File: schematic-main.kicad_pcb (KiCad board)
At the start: 2 copper layers, 100 x 100 mm, 145 parts, among them IC1 LM76202QPWPRQ1, IC2 AD8544ARUZ-REEL, IC3 ACHS-7123-000E, IC4 ACHS-7121-000E, IC5 ACHS-7123-000E, IC6 LM5106MMX_NOPB, J1 Battery converter, J2 CAN, J3 FUEL CELL, J4 Joulemeter, J5 MOTOR CONTROLER, J6 SUPER CAPACITORS, P1 USB_C_Plug_USB2.0, Q1 CSD19531Q5AT, Q2 CSD19531Q5AT, U1 TPS62933, U2 USBLC6-2P6, U3 ESP32-S3FN8, U4 SN65HVD232, Y1 Crystal_GND24

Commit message: Buck - boost converter
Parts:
- added C16: 100n, Capacitor_SMD:C_1206_3216Metric, F.Cu at (40.3, 160.3)
- added C17: 1u, Capacitor_SMD:C_1206_3216Metric, F.Cu at (35.0, 160.3)
- added C18: 1u, Capacitor_SMD:C_1206_3216Metric, F.Cu at (105.1, 133.8)
- added C22: 100n, Capacitor_SMD:C_1206_3216Metric, F.Cu at (28.2, 159.0)
- added C23: 100n, Capacitor_SMD:C_1206_3216Metric, F.Cu at (28.0, 164.0)
- added C24: 100n, Capacitor_SMD:C_1206_3216Metric, F.Cu at (31.9, 165.3)
- added C25: 1u, Capacitor_SMD:C_1206_3216Metric, F.Cu at (39.1, 174.5)
- added C26: 10n, Capacitor_SMD:C_1206_3216Metric, F.Cu at (44.0, 160.1)
- added C27: 4n7, Capacitor_SMD:C_1206_3216Metric, F.Cu at (30.7, 159.0)
- added C28: 100n, Capacitor_SMD:C_1206_3216Metric, F.Cu at (25.7, 159.0)
- added C31: 100n, Capacitor_SMD:C_1206_3216Metric, F.Cu at (123.4, 104.3)
- added C34: 1n, Capacitor_SMD:C_1206_3216Metric, F.Cu at (104.9, 99.6)
- added C47: 470n, Capacitor_SMD:C_1206_3216Metric, F.Cu at (238.5, 111.3)
- added C48: 10n, Capacitor_SMD:C_1206_3216Metric, F.Cu at (238.5, 114.6)
- added C49: 100n 100V, Capacitor_SMD:C_1206_3216Metric, F.Cu at (238.5, 118.0)
- added D10: 1N4148, Diode_THT:D_DO-35_SOD27_P7.62mm_Horizontal, F.Cu at (231.6, 100.7)
- added D11: 1N4148, Diode_THT:D_DO-35_SOD27_P7.62mm_Horizontal, F.Cu at (231.6, 104.3)
- added D12: 1N4148, Diode_THT:D_DO-35_SOD27_P7.62mm_Horizontal, F.Cu at (231.6, 107.8)
- added D4: LED, Package_TO_SOT_SMD:SOT-323_SC-70, F.Cu at (104.6, 95.4)
- added D5: LED, LED_SMD:LED_1206_3216Metric, F.Cu at (52.2, 165.3)
- added D6: LED, LED_SMD:LED_1206_3216Metric, F.Cu at (52.3, 168.4)
- added IC7: LM5106MMX_NOPB, Lib:SOP50P490X110-10N, F.Cu at (223.8, 117.3)
- added L3: 700uH, Inductor_SMD:L_0402_1005Metric, F.Cu at (30.8, 163.1)
- added Q3: CSD19531Q5AT, Lib:CSD19531Q5AT, F.Cu at (152.1, 92.9)
- added Q4: CSD19531Q5AT, Lib:CSD19531Q5AT, F.Cu at (163.9, 98.1)
- added R1: 5k1, Resistor_SMD:R_1206_3216Metric, F.Cu at (109.9, 138.8)
- added R2: 0, Resistor_SMD:R_1206_3216Metric, F.Cu at (105.2, 138.1)
- added R25: 10k, Resistor_SMD:R_1206_3216Metric, F.Cu at (26.1, 171.5)
- added R26: 10k, Resistor_SMD:R_1206_3216Metric, F.Cu at (26.1, 174.5)
- added R27: 20k, Resistor_SMD:R_1206_3216Metric, F.Cu at (30.0, 177.1)
- added R28: 10k, Resistor_SMD:R_1206_3216Metric, F.Cu at (33.1, 180.4)
- added R29: 20k, Resistor_SMD:R_1206_3216Metric, F.Cu at (35.2, 177.5)
- added R3: 0, Resistor_SMD:R_1206_3216Metric, F.Cu at (102.4, 138.1)
- added R30: 10k, Resistor_SMD:R_1206_3216Metric, F.Cu at (38.1, 180.5)
- added R31: 20k, Resistor_SMD:R_1206_3216Metric, F.Cu at (106.5, 102.2)
- added R32: 68k, Resistor_SMD:R_1206_3216Metric, F.Cu at (109.5, 104.7)
- added R35: 100R 0,5W, Resistor_SMD:R_1206_3216Metric, F.Cu at (57.5, 165.3)
- added R36: 100R 0,5W, Resistor_SMD:R_1206_3216Metric, F.Cu at (57.5, 168.4)
- added R4: 5k1, Resistor_SMD:R_1206_3216Metric, F.Cu at (97.6, 138.8)
- added R43: 100R, Resistor_SMD:R_1206_3216Metric, F.Cu at (242.9, 126.8)
- added R44: 10k, LED_SMD:LED_1206_3216Metric, F.Cu at (242.9, 123.5)
- added R45: 10R 2W, LED_SMD:LED_1206_3216Metric, F.Cu at (232.9, 111.3)
- added R46: 10k, LED_SMD:LED_1206_3216Metric, F.Cu at (232.9, 114.7)
- added R47: 10R 2W, Resistor_SMD:R_1206_3216Metric, F.Cu at (54.7, 160.2)
- added R48: 200R, Resistor_SMD:R_1206_3216Metric, F.Cu at (48.9, 160.1)
- added R49: 200R, LED_SMD:LED_1206_3216Metric, F.Cu at (232.9, 118.1)
- added R50: 0R, LED_SMD:LED_1206_3216Metric, F.Cu at (203.4, 67.2)
- added R51: 0R, LED_SMD:LED_1206_3216Metric, F.Cu at (203.4, 70.6)
- added TP10: I/O 2, Connector_PinSocket_2.54mm:PinSocket_1x01_P2.54mm_Vertical, F.Cu at (21.2, 169.8)
- added TP11: I/O 3, Connector_PinSocket_2.54mm:PinSocket_1x01_P2.54mm_Vertical, F.Cu at (21.2, 174.0)
- added TP12: I/O 4, Connector_PinSocket_2.54mm:PinSocket_1x01_P2.54mm_Vertical, F.Cu at (22.5, 178.0)
- added TP13: FC test, Connector_PinSocket_2.54mm:PinSocket_1x01_P2.54mm_Vertical, F.Cu at (26.5, 180.5)
- added TP20: I/O 4, Connector_PinSocket_2.54mm:PinSocket_1x01_P2.54mm_Vertical, F.Cu at (248.0, 127.5)
- added TP21: EN test, Connector_PinSocket_2.54mm:PinSocket_1x01_P2.54mm_Vertical, F.Cu at (243.1, 101.3)
- added TP22: PWM test, Connector_PinSocket_2.54mm:PinSocket_1x01_P2.54mm_Vertical, F.Cu at (243.1, 105.9)
- added U4: SN65HVD232, Package_DFN_QFN:QFN-56-1EP_7x7mm_P0.4mm_EP5.6x5.6mm, F.Cu at (39.8, 167.4)
- added U5: SN65HVD232, Package_SO:SOIC-8_3.9x4.9mm_P1.27mm, F.Cu at (116.7, 106.1)
- added Y1: Crystal_GND24, library:KC3225K400000C1GE00, F.Cu at (39.0, 156.6)
- J2: footprint Lib:39303035 -> library:39303035
- U3: footprint Package_DFN_QFN:QFN-56-1EP_7x7mm_P0.4mm_EP5.6x5.6mm -> Package_TO_SOT_SMD:SOT-666
- moved C32 29.0 mm to (150.5, 60.5)
- moved C45 21.5 mm to (151.0, 104.3), turned to 180 degrees
- moved L1 19.5 mm to (112.7, 75.3)
- moved U1 19.5 mm to (111.4, 80.3)
- moved U3 14.0 mm to (103.6, 130.8), turned to -90 degrees
- moved IC5 10.9 mm to (167.9, 125.2), turned to -90 degrees
- moved Q1 10.2 mm to (162.3, 73.1), turned to 90 degrees
- moved IC3 8.91 mm to (165.0, 109.4), turned to 90 degrees
- moved Q2 4.72 mm to (151.8, 73.1)
- moved F2 3.04 mm to (180.0, 122.0)
- moved J1 2.55 mm to (98.8, 80.0)
- moved J2 2.00 mm to (98.8, 97.4)
- moved P1 0.12 mm to (103.9, 145.9)
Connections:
- net /Converter/Bootstrap renamed /Converter/Bootstrap_A
- net /Converter/High_mosfet renamed /Converter/High_mosfet_A
- net /Converter/Low_mosfet renamed /Converter/Low_mosfet_A
- C44 pad 1: /Converter/SC_c2 -> /Converter/Bootstrap_B
- L3 pad 2: /Converter/SC_c2 -> /Converter/Bootstrap_B
- R35 pad 1: /Converter/SC_c2 -> /Converter/Bootstrap_B
- R39 pad 1: /Converter/Converter_ON_MCU -> /Converter/Converter_ON_B_MCU
- R40 pad 2: /Converter/Converter_PWM_MCU -> /Converter/Converter_PWM_B_MCU
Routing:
- net GND: track 0.00 -> 193.8 mm, vias 0 -> 25
- net (no net): track 0.00 -> 126.2 mm, vias 0 -> 9
- net +3.3V: track 0.00 -> 114.6 mm, vias 0 -> 5
- net /Converter/MC_c2: track 0.00 -> 90.6 mm
- net /Converter/SC_c2: track 0.00 -> 84.8 mm
- net /Converter/MC_c1: track 0.00 -> 50.8 mm
- net /Converter/FC_c1: track 0.00 -> 46.1 mm
- net /Converter/SC_c1: track 0.00 -> 45.7 mm
- net /IO/CAN_TX: track 0.00 -> 37.3 mm, vias 0 -> 1
- net /IO/CANH: track 0.00 -> 35.6 mm, vias 0 -> 1
- net unconnected-(U4-NC-Pad8): track 0.00 -> 34.3 mm, vias 0 -> 1
- net /IO/FC_Voltage_MCU: track 0.00 -> 32.1 mm, vias 0 -> 1
- net /Converter/FC_c2: track 0.00 -> 28.0 mm
- net /VBUS: track 0.00 -> 26.7 mm, vias 0 -> 2
- net /IO/CAN_RX: track 0.00 -> 21.1 mm
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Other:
- outline, holes or cut-outs redrawn

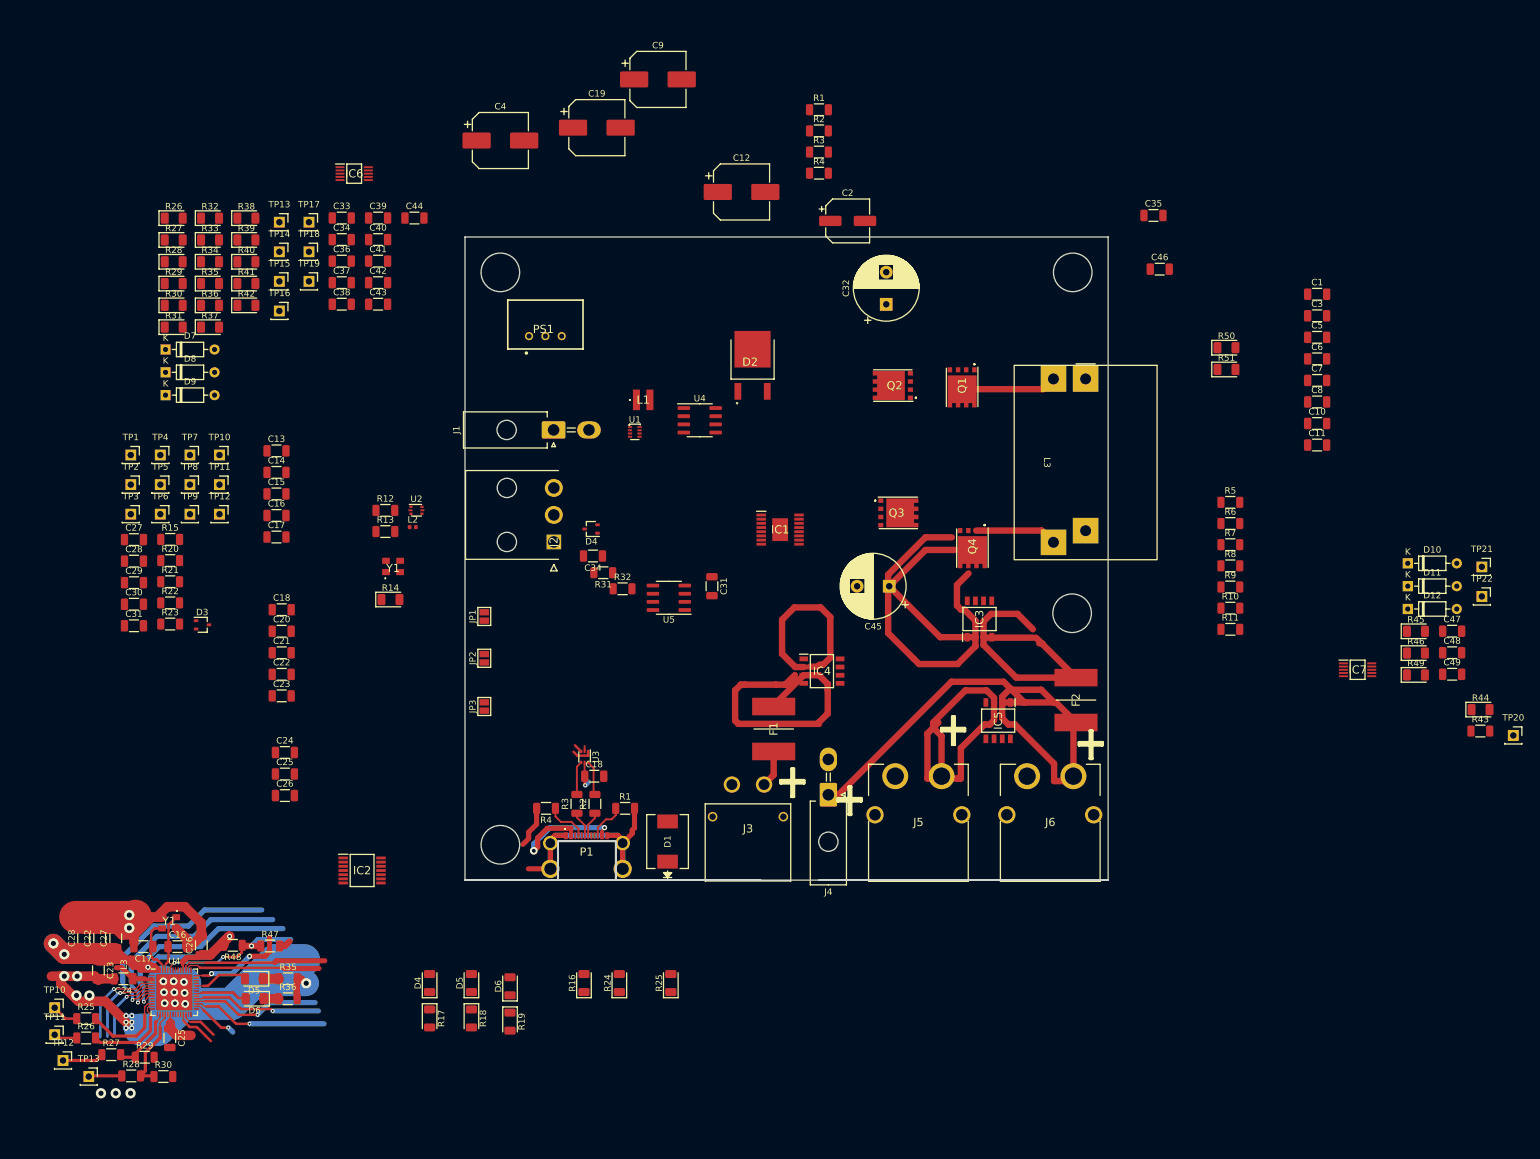
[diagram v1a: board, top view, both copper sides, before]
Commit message: Add coil and microcontroler
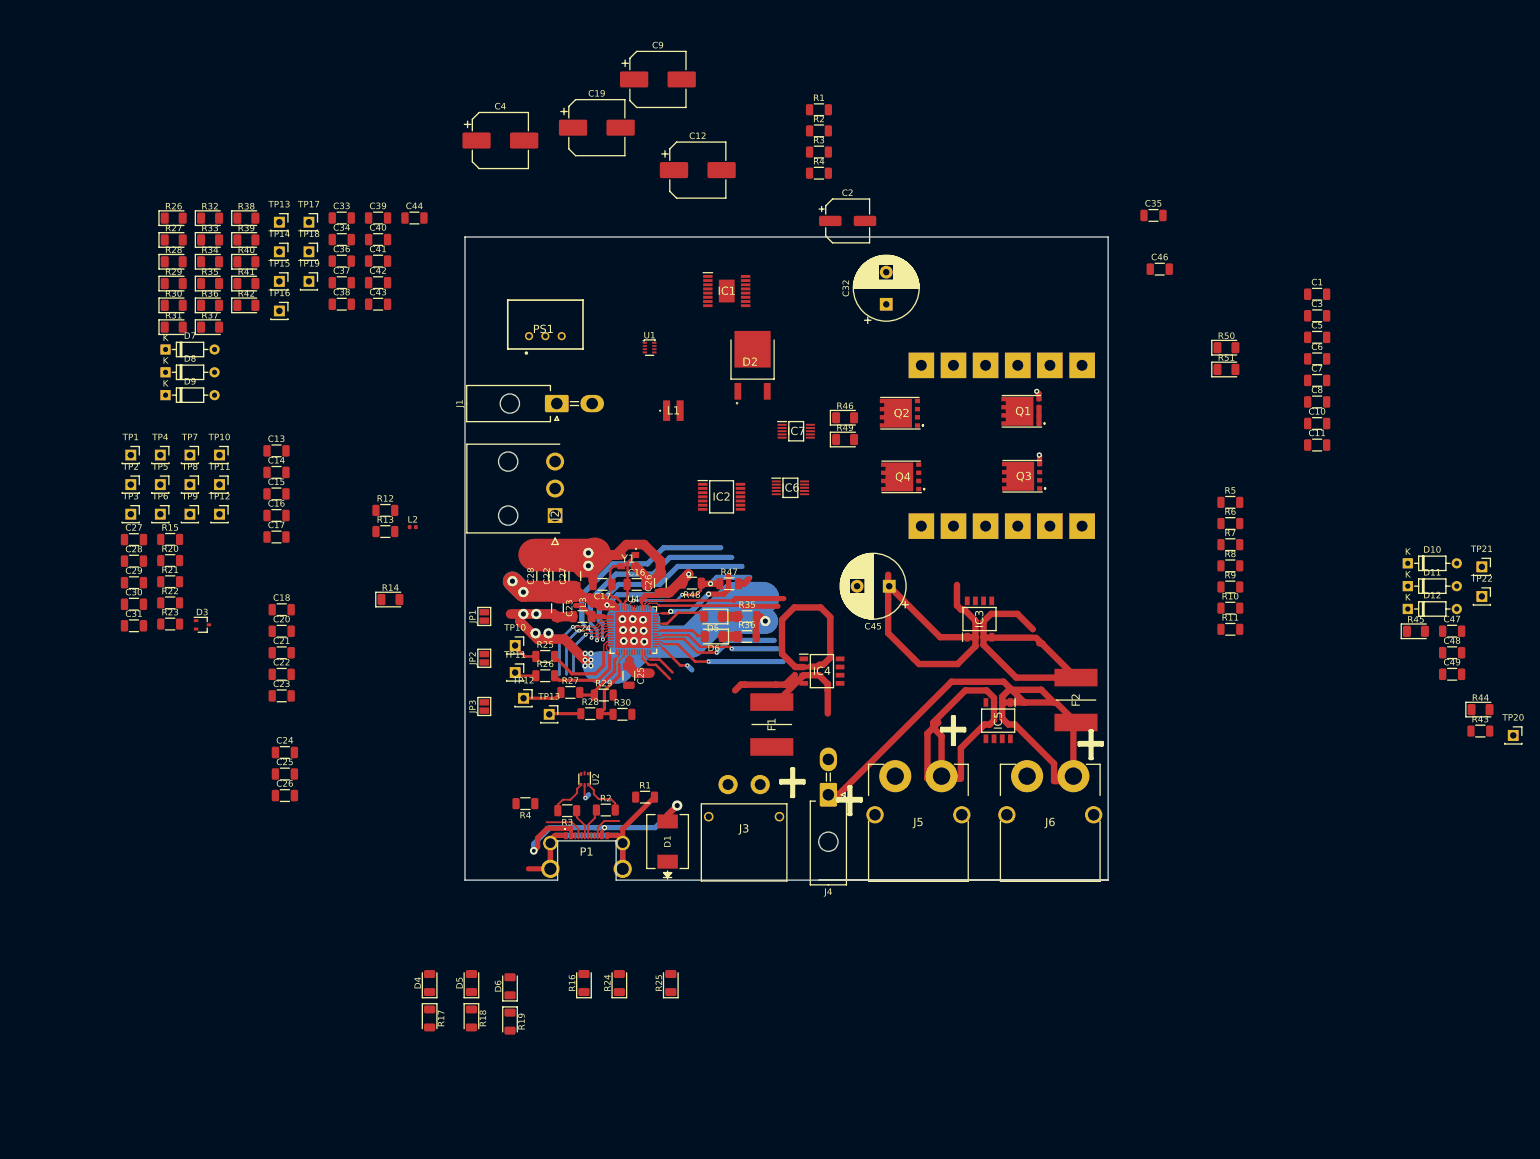
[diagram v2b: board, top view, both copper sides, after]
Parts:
- removed the C18 at (105.1, 133.8)
- removed the C31 at (123.4, 104.3)
- removed the C34 at (104.9, 99.6)
- removed the D4 at (104.6, 95.4)
- removed the R31 at (106.5, 102.2)
- removed the R32 at (109.5, 104.7)
- removed U3: ESP32-S3FN8, Package_TO_SOT_SMD:SOT-666
- removed the U4 at (121.5, 78.5)
- removed U5: SN65HVD232, Package_SO:SOIC-8_3.9x4.9mm_P1.27mm
- removed the Y1 at (73.8, 101.2)
- L3: moved to B.Cu
- moved R46 96.0 mm to (144.1, 78.1)
- moved R49 96.0 mm to (144.1, 81.5)
- moved IC7 94.8 mm to (136.5, 80.2)
- moved TP10 91.1 mm to (92.8, 113.5)
- moved TP11 91.1 mm to (92.8, 117.7)
- moved TP12 91.1 mm to (94.1, 121.7)
- moved TP13 91.1 mm to (98.1, 124.2)
- moved C16 90.9 mm to (111.7, 104.0)
- moved D6 90.9 mm to (123.7, 112.1)
- moved L3 90.9 mm to (102.2, 106.8)
- moved R36 90.9 mm to (128.8, 112.1)
- moved U4 90.9 mm to (111.2, 111.1)
- moved C17 90.9 mm to (106.4, 104.0)
- moved C22 90.9 mm to (99.6, 102.7)
- moved C23 90.9 mm to (99.4, 107.7)
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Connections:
- J3 pad 1: /Converter/FC+ -> GND
- J3 pad 2: GND -> /Converter/FC+
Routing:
- net (no net): track 126.2 -> 86.0 mm, vias 9 -> 7
- net /Converter/SC_c2: track 84.8 -> 53.5 mm
- net Net-(P1-VCONN): track 5.91 -> 27.6 mm
- net /IO/CAN_RX: track 21.1 -> 0.00 mm
- net GND: track 193.8 -> 214.0 mm, vias 25 -> 22
- net /Converter/FC_c1: track 46.1 -> 26.0 mm
- net unconnected-(U4-NC-Pad5): track 13.2 -> 33.1 mm, vias 1 -> 2
- net /VBUS: track 26.7 -> 44.0 mm, vias 2 -> 3
- net /Converter/Bootstrap_A: track 14.9 -> 0.00 mm
- net /Converter/Bootstrap_B: track 12.8 -> 0.00 mm
- net /Converter/FC+: track 5.77 -> 0.14 mm
- net +3.3V: track 114.6 -> 111.1 mm
- net unconnected-(U3-LNA_IN/RF-Pad1): track 3.17 -> 0.00 mm
- net /IO/CAN_TX: track 37.3 -> 34.8 mm, vias 1 -> 2
- net VDD3P3: track 11.1 -> 8.96 mm
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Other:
- outline, holes or cut-outs redrawn

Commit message: Add pot
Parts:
- removed C1, C13, C18, C20: 1u, Capacitor_SMD:C_1206_3216Metric
- removed C10: 47p, Capacitor_SMD:C_1206_3216Metric
- removed C11, C21, C31, C33, C35, C37, C6, C7, C8: 100n, Capacitor_SMD:C_1206_3216Metric
- removed C12: 100u, Capacitor_SMD:CP_Elec_8x10.5
- removed C14, C15: 12p, Capacitor_SMD:C_1206_3216Metric
- removed the C16 at (111.7, 104.0)
- removed the C16 at (55.7, 93.3)
- removed the C17 at (106.4, 104.0)
- removed the C17 at (55.7, 96.7)
- removed C19, C4, C9: 10u, Capacitor_SMD:CP_Elec_8x10.5
- removed C2: 47u, Capacitor_SMD:CP_Elec_6.3x7.7
- removed the C22 at (99.6, 102.7)
- removed the C22 at (56.5, 118.0)
- removed the C23 at (99.4, 107.7)
- removed the C23 at (56.5, 121.3)
- removed the C24 at (57.0, 130.2)
- removed the C24 at (103.3, 109.0)
- removed the C25 at (57.0, 133.5)
- removed the C25 at (110.5, 118.2)
- removed the C26 at (57.0, 136.8)
- removed the C26 at (115.4, 103.8)
- removed the C27 at (33.5, 97.0)
- removed the C27 at (102.1, 102.7)
- removed the C28 at (97.1, 102.7)
- removed the C28 at (33.5, 100.4)
- removed C29, C30: 4n7, Capacitor_SMD:C_1206_3216Metric
- removed C3: 2n7, Capacitor_SMD:C_1206_3216Metric
- removed C34, C36, C38, C39, C46: 1n, Capacitor_SMD:C_1206_3216Metric
- removed C40, C47: 470n, Capacitor_SMD:C_1206_3216Metric
- removed C41, C48: 10n, Capacitor_SMD:C_1206_3216Metric
- removed C42, C49: 100n 100V, Capacitor_SMD:C_1206_3216Metric
- removed C43, C44: 100p 100V, Capacitor_SMD:C_1206_3216Metric
- removed C5: 33n, Capacitor_SMD:C_1206_3216Metric
- removed D10, D11, D12, D7, D8, D9: 1N4148, Diode_THT:D_DO-35_SOD27_P7.62mm_Horizontal
- removed D3: SP0502BAJT, Package_TO_SOT_SMD:SOT-323_SC-70
- removed D4: LED, Diode_SMD:D_1206_3216Metric
- removed the D5 at (86.0, 166.0)
- removed the D5 at (123.6, 109.0)
- removed the D6 at (123.7, 112.1)
- removed the D6 at (92.0, 166.5)
- removed JP1, JP2, JP3: SolderJumper_2_Open, Jumper:SolderJumper-2_P1.3mm_Open_Pad1.0x1.5mm
- removed L2: 2n, Inductor_SMD:L_0402_1005Metric
- removed the R1 at (140.0, 30.2)
- removed R10: 32k, Resistor_SMD:R_1206_3216Metric
- removed R11, R12, R13: 10k, Resistor_SMD:R_1206_3216Metric
- removed R14, R24, R37, R44: 10k, LED_SMD:LED_1206_3216Metric
- removed R15: 60, Resistor_SMD:R_1206_3216Metric
- removed R16: 60, LED_SMD:LED_1206_3216Metric
- removed R17, R18, R19: 1k, LED_SMD:LED_1206_3216Metric
- removed the R2 at (140.0, 33.5)
- removed R20, R21: 1k, Resistor_SMD:R_1206_3216Metric
- removed R22, R23, R43: 100R, Resistor_SMD:R_1206_3216Metric
- removed the R25 at (117.0, 166.0)
- removed the R25 at (97.5, 115.2)
- removed the R26 at (39.7, 47.1)
- removed the R26 at (97.5, 118.2)
- removed the R27 at (39.7, 50.5)
- removed the R27 at (101.4, 120.8)
- removed the R28 at (104.5, 124.1)
- removed the R28 at (39.7, 53.9)
- removed the R29 at (39.7, 57.2)
- removed the R29 at (106.6, 121.2)
- removed the R3 at (140.0, 36.8)
- removed the R30 at (39.7, 60.6)
- removed the R30 at (109.5, 124.2)
- removed R31: 20k, LED_SMD:LED_1206_3216Metric
- removed R32: 68k, LED_SMD:LED_1206_3216Metric
- removed R33: 3k9, LED_SMD:LED_1206_3216Metric
- removed R34, R38, R45: 10R 2W, LED_SMD:LED_1206_3216Metric
- removed the R35 at (128.9, 109.0)
- removed the R35 at (45.4, 57.2)
- removed the R36 at (45.4, 60.6)
- removed the R36 at (128.8, 112.1)
- removed R39, R40: 200R, LED_SMD:LED_1206_3216Metric
- removed the R4 at (140.0, 40.1)
- removed R41: 62k, LED_SMD:LED_1206_3216Metric
- removed R42: 4k7, LED_SMD:LED_1206_3216Metric
- removed R5: 180k, Resistor_SMD:R_1206_3216Metric
- removed R50, R51: 0R, LED_SMD:LED_1206_3216Metric
- removed R6: 12k, Resistor_SMD:R_1206_3216Metric
- removed R7, R8: 100k, Resistor_SMD:R_1206_3216Metric
- removed R9: 56k, Resistor_SMD:R_1206_3216Metric
- removed TP10 (x2): I/O 2, Connector_PinSocket_2.54mm:PinSocket_1x01_P2.54mm_Vertical
- removed TP11 (x2): I/O 3, Connector_PinSocket_2.54mm:PinSocket_1x01_P2.54mm_Vertical
- removed the TP12 at (46.8, 93.1)
- removed the TP12 at (94.1, 121.7)
- removed the TP13 at (56.1, 47.7)
- removed the TP13 at (98.1, 124.2)
- removed TP14: FC_C_test, Connector_PinSocket_2.54mm:PinSocket_1x01_P2.54mm_Vertical
- removed TP15: SC_C_test, Connector_PinSocket_2.54mm:PinSocket_1x01_P2.54mm_Vertical
- removed TP16: MC_C_test, Connector_PinSocket_2.54mm:PinSocket_1x01_P2.54mm_Vertical
- removed TP17, TP21: EN test, Connector_PinSocket_2.54mm:PinSocket_1x01_P2.54mm_Vertical
- removed TP18, TP22: PWM test, Connector_PinSocket_2.54mm:PinSocket_1x01_P2.54mm_Vertical
- removed TP19: SC test, Connector_PinSocket_2.54mm:PinSocket_1x01_P2.54mm_Vertical
- removed the TP2 at (33.0, 88.5)
- removed TP20: I/O 4, Connector_PinSocket_2.54mm:PinSocket_1x01_P2.54mm_Vertical
- removed TP4: +12V, Connector_PinSocket_2.54mm:PinSocket_1x01_P2.54mm_Vertical
- removed TP5, TP6: +5V, Connector_PinSocket_2.54mm:PinSocket_1x01_P2.54mm_Vertical
- removed TP7, TP8: +3.3V, Connector_PinSocket_2.54mm:PinSocket_1x01_P2.54mm_Vertical
- removed TP9: I/O 1, Connector_PinSocket_2.54mm:PinSocket_1x01_P2.54mm_Vertical
- added C16: 12p, Capacitor_SMD:C_1206_3216Metric, F.Cu at (41.9, 166.2)
- added C17: 12p, Capacitor_SMD:C_1206_3216Metric, F.Cu at (36.6, 166.2)
- added C22: 1u, Capacitor_SMD:C_1206_3216Metric, F.Cu at (29.8, 164.9)
- added C23: 100n, Capacitor_SMD:C_1206_3216Metric, F.Cu at (29.6, 169.9)
- added C24: 100n, Capacitor_SMD:C_1206_3216Metric, F.Cu at (33.5, 171.2)
- added C25: 100n, Capacitor_SMD:C_1206_3216Metric, F.Cu at (40.7, 180.4)
- added C26: 100n, Capacitor_SMD:C_1206_3216Metric, F.Cu at (45.6, 166.0)
- added C27: 1u, Capacitor_SMD:C_1206_3216Metric, F.Cu at (32.3, 164.9)
- added C28: 10n, Capacitor_SMD:C_1206_3216Metric, F.Cu at (27.3, 164.9)
- added D5: LED, LED_SMD:LED_1206_3216Metric, F.Cu at (53.8, 171.2)
- added D6: LED, LED_SMD:LED_1206_3216Metric, F.Cu at (53.9, 174.3)
- added R25: 1k, Resistor_SMD:R_1206_3216Metric, F.Cu at (27.7, 177.4)
- added R26: 1k, Resistor_SMD:R_1206_3216Metric, F.Cu at (27.7, 180.4)
- added R27: 100R, Resistor_SMD:R_1206_3216Metric, F.Cu at (31.6, 183.0)
- added R28: 100R, Resistor_SMD:R_1206_3216Metric, F.Cu at (34.7, 186.3)
- added R29: 10k, Resistor_SMD:R_1206_3216Metric, F.Cu at (36.8, 183.4)
- added R30: 10k, Resistor_SMD:R_1206_3216Metric, F.Cu at (39.7, 186.4)
- added R35: 1k, Resistor_SMD:R_1206_3216Metric, F.Cu at (59.1, 171.2)
- added R36: 1k, Resistor_SMD:R_1206_3216Metric, F.Cu at (59.0, 174.3)
- added TP12: I/O 3, Connector_PinSocket_2.54mm:PinSocket_1x01_P2.54mm_Vertical, F.Cu at (24.1, 183.9)
- added TP13: I/O 4, Connector_PinSocket_2.54mm:PinSocket_1x01_P2.54mm_Vertical, F.Cu at (28.1, 186.4)
- added TP2: GND, Connector_PinSocket_2.54mm:PinSocket_1x01_P2.54mm_Vertical, F.Cu at (18.1, 160.3)
- added TP2: I/O 2, Connector_PinSocket_2.54mm:PinSocket_1x01_P2.54mm_Vertical, F.Cu at (22.8, 179.9)
- L3: value 700uH -> 2n
- R47: value 10R 2W -> 10k
- R48: value 200R -> 10k
- TP1: value GND -> I/O 1
- TP3: value +12V -> GND
- U4: value SN65HVD232 -> ESP32-S3FN8
- moved L3 93.5 mm to (32.4, 169.0)
- moved R48 93.5 mm to (50.5, 166.0)
- moved U4 93.5 mm to (41.4, 173.3)
- moved Y1 93.5 mm to (40.6, 162.5)
- moved R47 93.5 mm to (56.3, 166.1)
- moved TP1 92.4 mm to (22.8, 175.7)
- moved TP3 67.9 mm to (23.1, 160.3)
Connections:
- L3 pad 1: /Converter/Bootstrap_A -> +3.3V
- L3 pad 2: /Converter/Bootstrap_B -> VDD3P3
- R47 pad 1: /Converter/Low_mosfet_B -> (no net)
- R47 pad 2: Net-(D12-A) -> GND
- R48 pad 1: /Converter/Converter_ON_B_MCU -> (no net)
- R48 pad 2: Net-(IC7-EN) -> +3.3V
- TP1 pad 1: GND -> (no net)
- TP3 pad 1: +12V -> GND
- U4 pad 1: /IO/CAN_RX -> (no net)
- U4 pad 12: (no net) -> /IO/I/O_1_MCU
- U4 pad 13: (no net) -> /IO/I/O_2_MCU
- U4 pad 16: (no net) -> /IO/I/O_3_MCU
- U4 pad 18: (no net) -> /IO/I/O_4_MCU
- U4 pad 2: GND -> VDD3P3
- U4 pad 20: (no net) -> +3.3V
- U4 pad 25: (no net) -> /MCU/USB_D-
- U4 pad 26: (no net) -> /MCU/USB_D+
- U4 pad 3: +3.3V -> VDD3P3
- U4 pad 35: (no net) -> /IO/LED_MCU_STATUS
- U4 pad 38: (no net) -> /IO/LED_CAN_STATUS
- U4 pad 4: /IO/CAN_TX -> /MCU/RESET
- U4 pad 44: (no net) -> /IO/CAN_RX
- U4 pad 45: (no net) -> /IO/CAN_TX
- U4 pad 46: (no net) -> +3.3V
- U4 pad 5: unconnected-(U4-NC-Pad5) -> /MCU/BOOT
- U4 pad 53: (no net) -> /MCU/XTAL_N
- U4 pad 54: (no net) -> /MCU/XTAL_P
- U4 pad 55: (no net) -> +3.3V
- U4 pad 56: (no net) -> +3.3V
- U4 pad 57: (no net) -> GND
- U4 pad 6: /IO/CANL -> /MCU/MCU_TEST
- U4 pad 7: /IO/CANH -> (no net)
- U4 pad 8: unconnected-(U4-NC-Pad8) -> (no net)
- U4 pad 9: (no net) -> /IO/FC_Voltage_MCU
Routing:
- net (no net): track 86.0 -> 133.4 mm, vias 7 -> 11
- net /IO/CANH: track 35.6 -> 0.00 mm, vias 1 -> 0
- net unconnected-(U4-NC-Pad8): track 34.3 -> 0.00 mm, vias 1 -> 0
- net unconnected-(U4-NC-Pad5): track 33.1 -> 0.00 mm, vias 2 -> 0
- net /MCU/RESET: track 0.00 -> 29.7 mm, vias 0 -> 2
- net /MCU/BOOT: track 0.00 -> 28.6 mm, vias 0 -> 1
- net GND: track 214.0 -> 185.9 mm, vias 22 -> 21
- net /MCU/MCU_TEST: track 0.00 -> 25.8 mm, vias 0 -> 1
- net Net-(P1-VCONN): track 27.6 -> 5.04 mm
- net /IO/FC_Voltage_MCU: track 32.1 -> 11.8 mm
- net /IO/CAN_TX: track 34.8 -> 15.1 mm, vias 2 -> 0
- net /IO/CAN_RX: track 0.00 -> 15.7 mm
- net /Converter/FC_c2: track 28.0 -> 13.8 mm
- net Net-(IC3-VOUT): track 14.2 -> 0.00 mm
- net /IO/I/O_2_MCU: track 0.00 -> 14.2 mm
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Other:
- board text added: "2x GND"
- board text added: "Fuel Cell Unit v1 Michał Borkowski 05.03.2024"
- board text added: "I/O 1 I/O 2"
- board text added: "I/O 3 I/O 4"
